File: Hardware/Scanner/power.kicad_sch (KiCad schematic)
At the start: 16 parts, among them J1 I2C ThroughHole, J2 Conn_01x09, J3 SM04B-SRSS-TB, J4 Interface, U10 AP2127N-1.8, U9 AP2127N-2.5

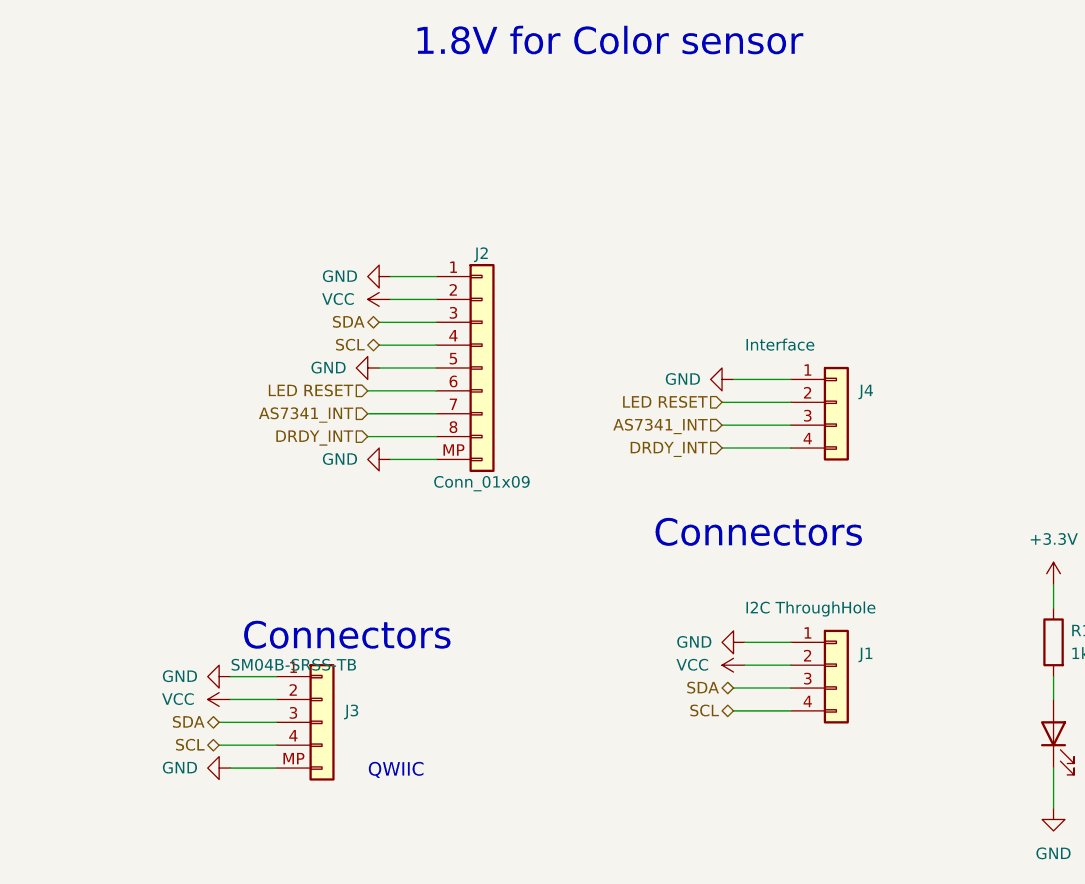
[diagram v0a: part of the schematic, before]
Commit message: cleared all DRC errors
Signed-off-by: lokimetasmith <lokimail@gmail.com>
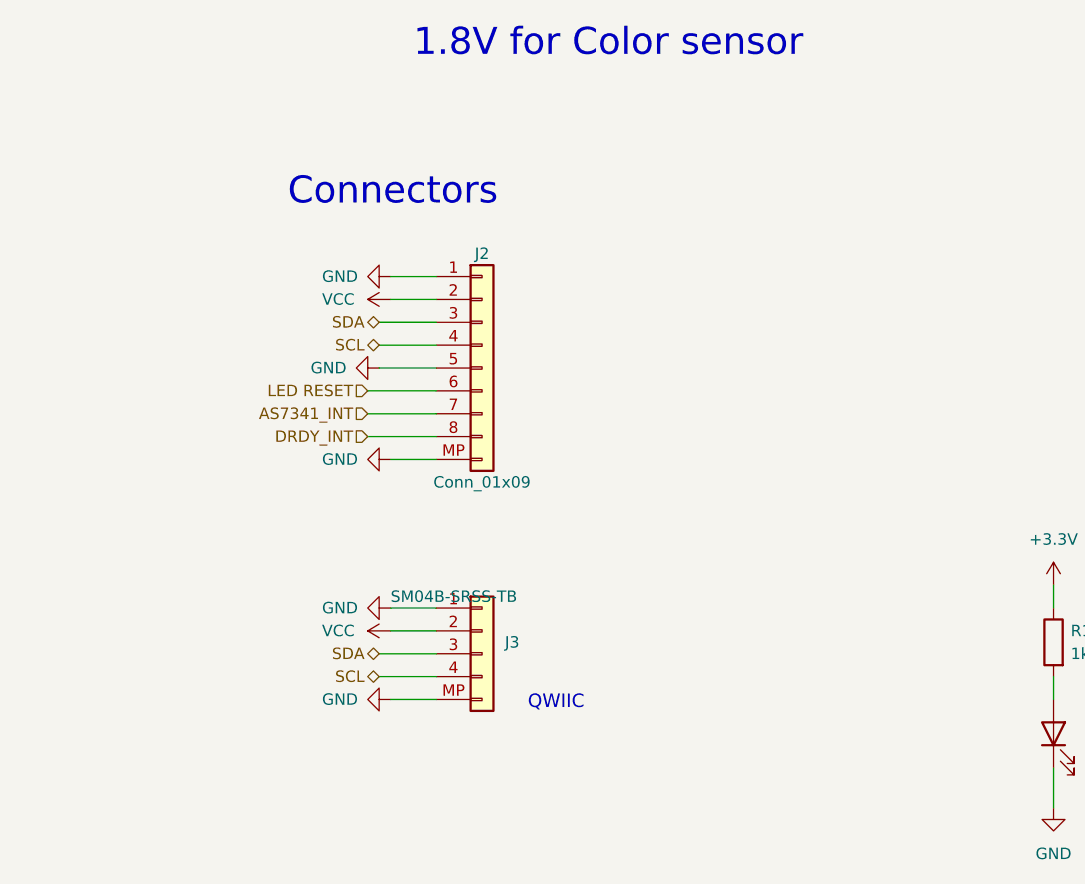
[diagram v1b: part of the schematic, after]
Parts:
- removed J1: I2C ThroughHole, Connector_PinSocket_2.54mm:PinSocket_1x04_P2.54mm_Vertical, symbol Connector_Generic:Conn_01x04
- removed J4: Interface, Connector_PinSocket_2.54mm:PinSocket_1x04_P2.54mm_Vertical, symbol Connector_Generic:Conn_01x04
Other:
- moved on the sheet: J3
